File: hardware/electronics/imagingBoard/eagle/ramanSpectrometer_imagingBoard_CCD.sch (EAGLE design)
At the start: 3 parts

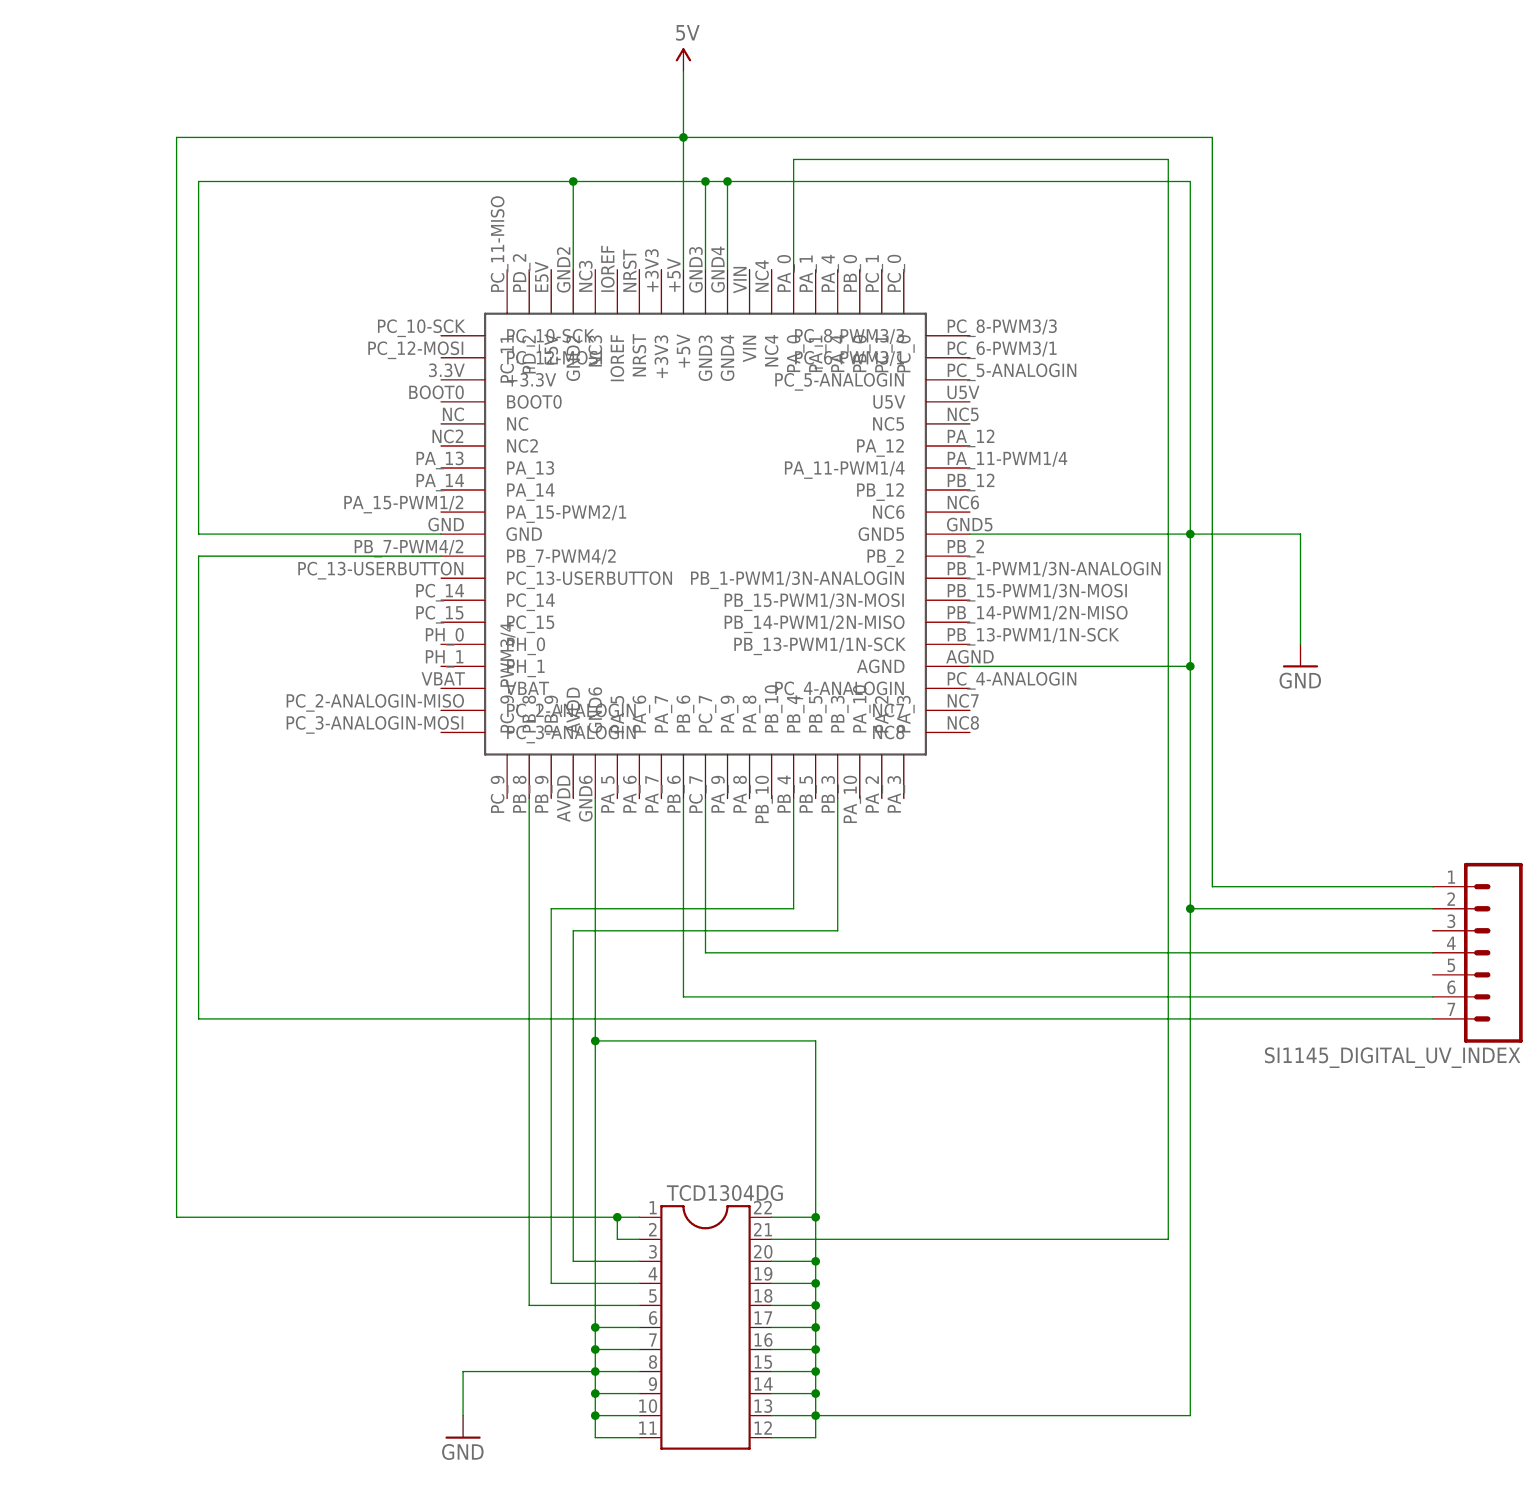
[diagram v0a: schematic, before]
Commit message: updated imagingBoard schematic
Added DS18B20 to schematic
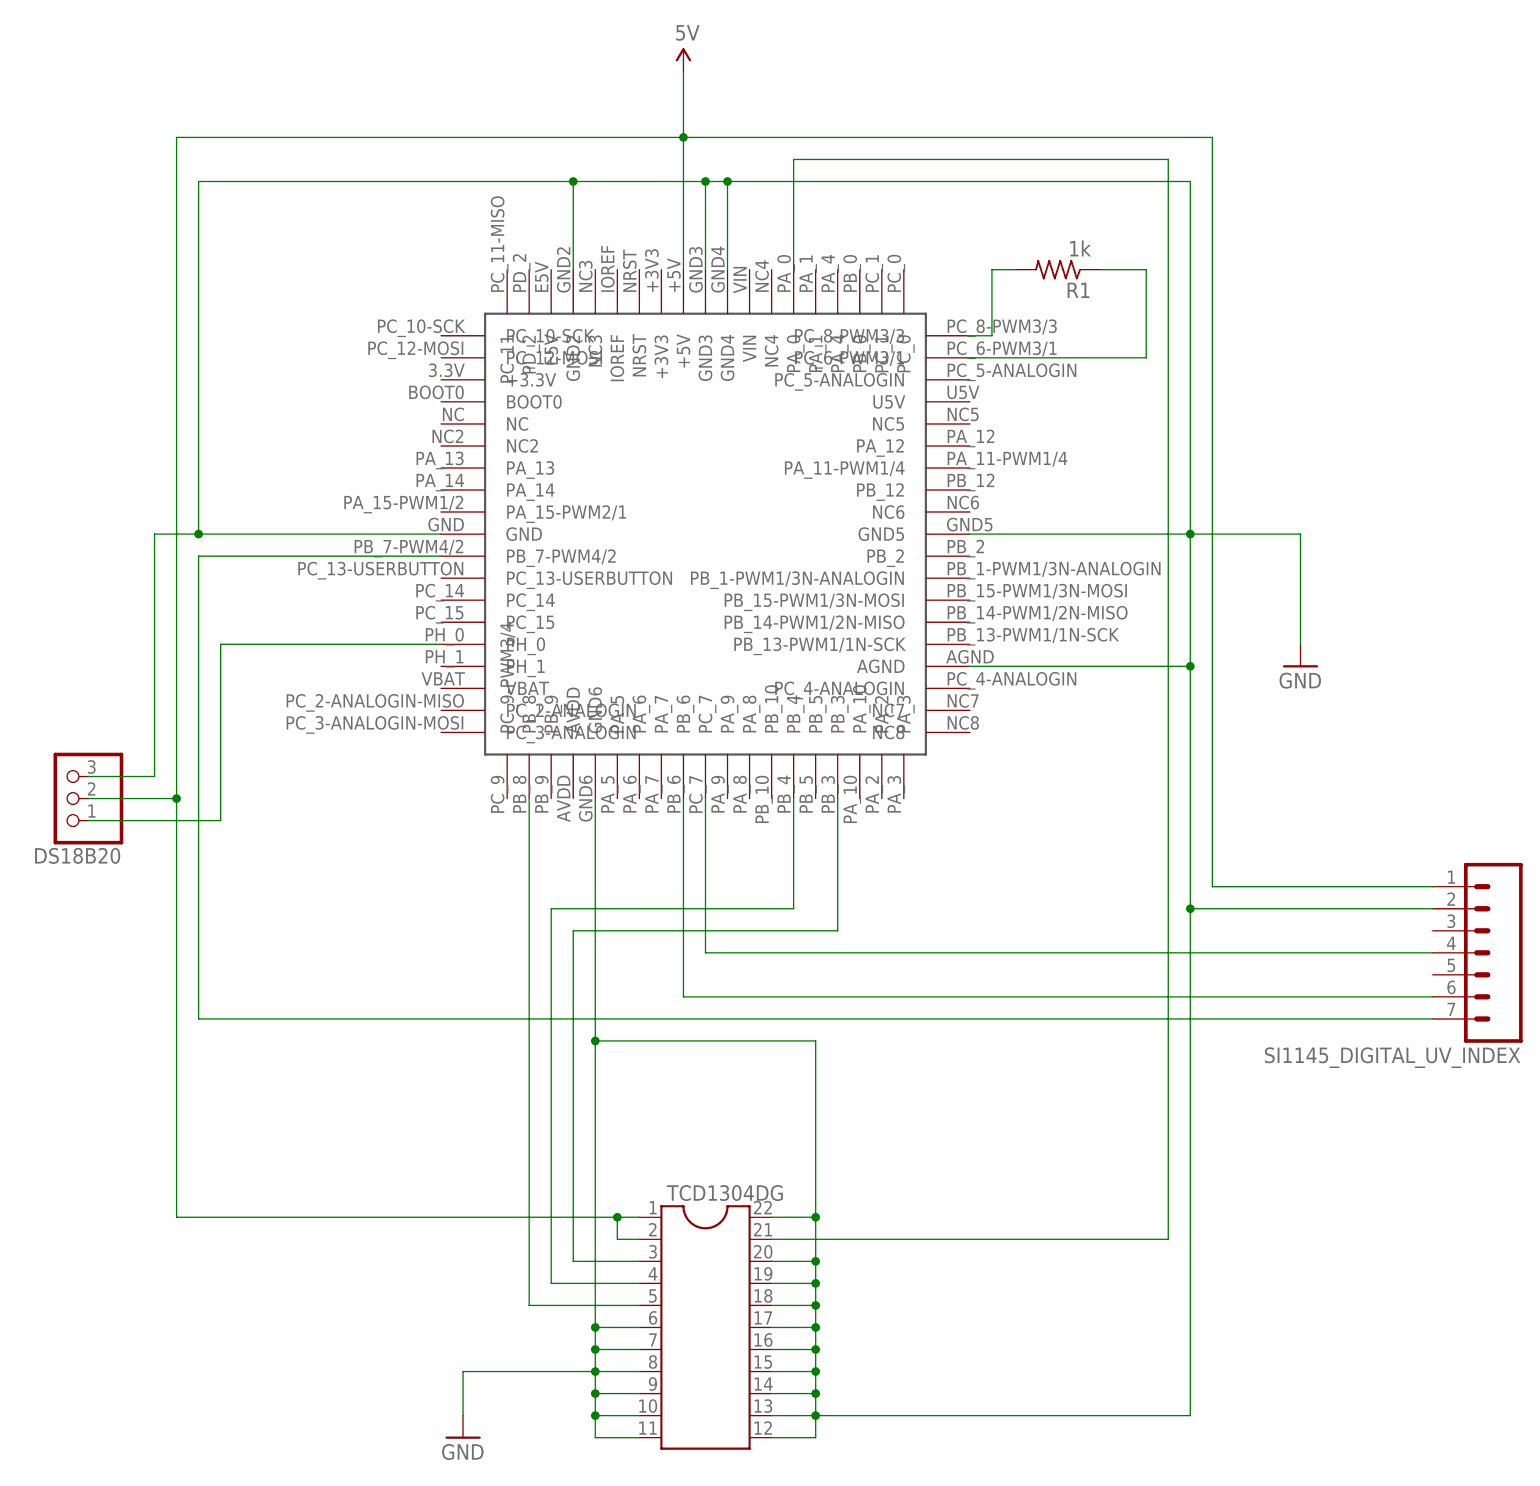
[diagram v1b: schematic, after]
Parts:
- added DS18B20: (no value), adafruit:PINHD-1X3
- added R1: 1k, adafruit:R-US_M1206
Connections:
- new net N$4: R1.2, U$1.PC_8-PWM3/3
- new net N$5: R1.1, U$1.PC_6-PWM3/1
- new net N$6: DS18B20.1, U$1.PH_0
- net 5V: now also DS18B20.2
- net GND: now also DS18B20.3
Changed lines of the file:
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@@
 <part name="GND1" library="SparkFun-Aesthetics" deviceset="GND" device=""/>
 <part name="GND2" library="SparkFun-Aesthetics" deviceset="GND" device=""/>
+<part name="R1" library="adafruit" deviceset="R-US_" device="M1206" value="1k"/>
+<part name="DS18B20" library="adafruit" deviceset="PINHD-1X3" device=""/>
 </parts>
 <sheets>
@@
 <instance part="GND1" gate="1" x="50.8" y="30.48"/>
 <instance part="GND2" gate="1" x="147.32" y="119.38"/>
+<instance part="R1" gate="G$1" x="119.38" y="165.1" rot="R180"/>
+<instance part="DS18B20" gate="A" x="5.08" y="104.14" rot="R180"/>
 </instances>
 <busses>
@@
 <wire x1="66.04" y1="38.1" x2="50.8" y2="38.1" width="0.1524" layer="91"/>
 <wire x1="50.8" y1="38.1" x2="50.8" y2="33.02" width="0.1524" layer="91"/>
+<wire x1="7.62" y1="106.68" x2="15.24" y2="106.68" width="0.1524" layer="91"/>
+<wire x1="15.24" y1="106.68" x2="15.24" y2="134.62" width="0.1524" layer="91"/>
+<wire x1="15.24" y1="134.62" x2="20.32" y2="134.62" width="0.1524" layer="91"/>
+<junction x="20.32" y="134.62"/>
+<pinref part="DS18B20" gate="A" pin="3"/>
 </segment>
 </net>
@@
 <wire x1="71.12" y1="55.88" x2="68.58" y2="55.88" width="0.1524" layer="91"/>
 <wire x1="68.58" y1="55.88" x2="17.78" y2="55.88" width="0.1524" layer="91"/>
-<wire x1="17.78" y1="55.88" x2="17.78" y2="180.34" width="0.1524" layer="91"/>
 <pinref part="U$1" gate="G$1" pin="+5V"/>
+<wire x1="17.78" y1="55.88" x2="17.78" y2="104.14" width="0.1524" layer="91"/>
+<wire x1="17.78" y1="104.14" x2="17.78" y2="180.34" width="0.1524" layer="91"/>
 <wire x1="17.78" y1="180.34" x2="76.2" y2="180.34" width="0.1524" layer="91"/>
 <wire x1="76.2" y1="180.34" x2="76.2" y2="165.1" width="0.1524" layer="91"/>
@@
 <pinref part="SUPPLY1" gate="G$1" pin="5V"/>
 <wire x1="76.2" y1="180.34" x2="76.2" y2="187.96" width="0.1524" layer="91"/>
-</segment>
-</net>
+<wire x1="7.62" y1="104.14" x2="17.78" y2="104.14" width="0.1524" layer="91"/>
+<junction x="17.78" y="104.14"/>
+<pinref part="DS18B20" gate="A" pin="2"/>
+</segment>
+</net>
+<net name="N$4" class="0">
+<segment>
+<pinref part="U$1" gate="G$1" pin="PC_8-PWM3/3"/>
+<wire x1="109.22" y1="157.48" x2="111.76" y2="157.48" width="0.1524" layer="91"/>
+<wire x1="111.76" y1="157.48" x2="111.76" y2="165.1" width="0.1524" layer="91"/>
+<pinref part="R1" gate="G$1" pin="2"/>
+<wire x1="111.76" y1="165.1" x2="114.3" y2="165.1" width="0.1524" layer="91"/>
+</segment>
+</net>
+<net name="N$5" class="0">
+<segment>
+<pinref part="U$1" gate="G$1" pin="PC_6-PWM3/1"/>
+<wire x1="109.22" y1="154.94" x2="129.54" y2="154.94" width="0.1524" layer="91"/>
+<wire x1="129.54" y1="154.94" x2="129.54" y2="165.1" width="0.1524" layer="91"/>
+<pinref part="R1" gate="G$1" pin="1"/>
+<wire x1="129.54" y1="165.1" x2="124.46" y2="165.1" width="0.1524" layer="91"/>
+</segment>
+</net>
+<net name="N$6" class="0">
+<segment>
+<pinref part="U$1" gate="G$1" pin="PH_0"/>
+<wire x1="22.86" y1="121.92" x2="48.26" y2="121.92" width="0.1524" layer="91"/>
+<wire x1="22.86" y1="121.92" x2="22.86" y2="101.6" width="0.1524" layer="91"/>
+<wire x1="22.86" y1="101.6" x2="7.62" y2="101.6" width="0.1524" layer="91"/>
+<pinref part="DS18B20" gate="A" pin="1"/>
+</segment>
+</net>
